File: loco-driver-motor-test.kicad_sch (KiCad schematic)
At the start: 1 part, among them J101 Conn_02x09_Odd_Even

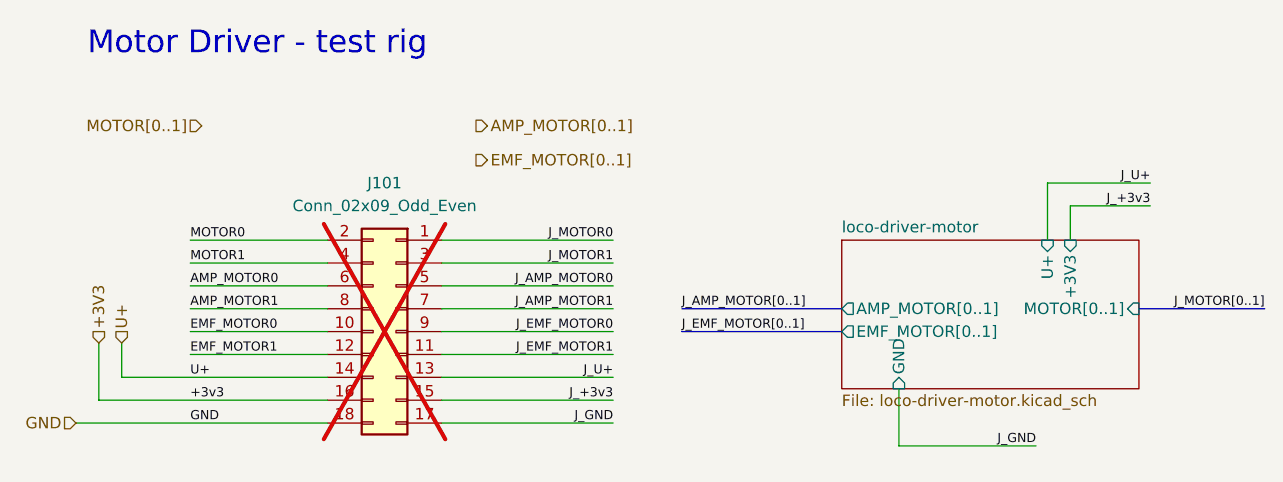
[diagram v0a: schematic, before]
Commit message: Fix - loco-driver-motor-tests pins
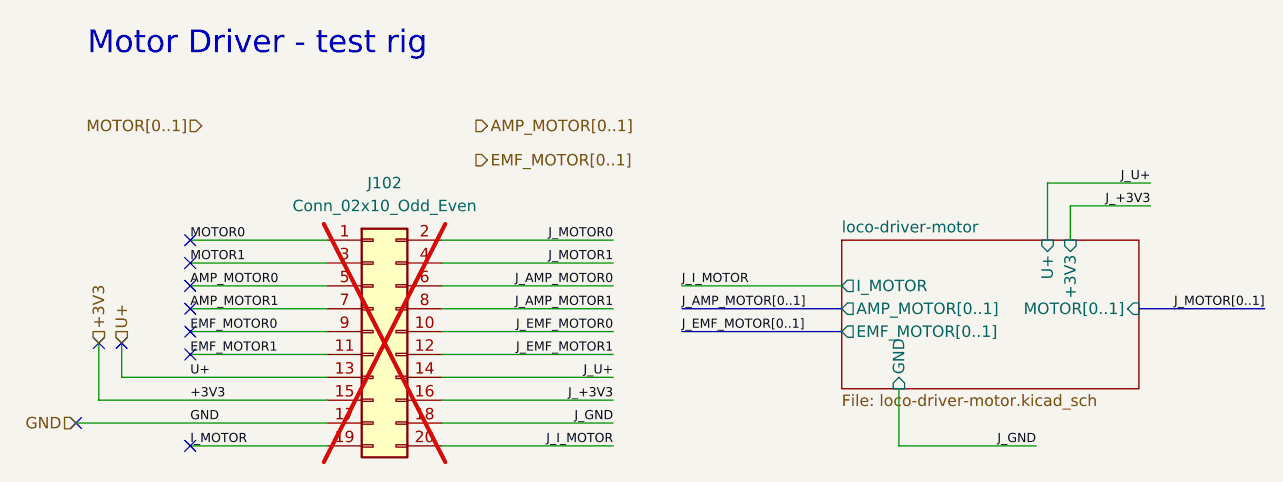
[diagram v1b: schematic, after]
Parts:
- removed J101: Conn_02x09_Odd_Even, Connector_PinSocket_2.54mm:PinSocket_2x09_P2.54mm_Vertical, symbol Connector_Generic:Conn_02x09_Odd_Even
- added J102: Conn_02x10_Odd_Even, Connector_PinSocket_2.54mm:PinSocket_2x10_P2.54mm_Vertical, symbol Connector_Generic:Conn_02x10_Odd_Even
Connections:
- net +3V3: now also J102.15 (Pin_15)
- net AMP_MOTOR0: now also J102.5 (Pin_5)
- net AMP_MOTOR1: now also J102.7 (Pin_7)
- net EMF_MOTOR0: now also J102.9 (Pin_9)
- net EMF_MOTOR1: now also J102.11 (Pin_11)
- net GND: now also J102.17 (Pin_17)
- net J_AMP_MOTOR0: now also J102.6 (Pin_6)
- net J_AMP_MOTOR1: now also J102.8 (Pin_8)
- net J_EMF_MOTOR0: now also J102.10 (Pin_10)
- net J_EMF_MOTOR1: now also J102.12 (Pin_12)
- net J_GND: now also J102.18 (Pin_18)
- net J_MOTOR0: now also J102.2 (Pin_2)
- net J_MOTOR1: now also J102.4 (Pin_4)
- net J_U+: now also J102.14 (Pin_14)
- net MOTOR0: now also J102.1 (Pin_1)
- net MOTOR1: now also J102.3 (Pin_3)
- net U+: now also J102.13 (Pin_13)
- new net I_MOTOR: J102.19 (Pin_19)
- new net J_+3V3: J102.16 (Pin_16)
- new net J_I_MOTOR: J102.20 (Pin_20)
- no-connect marks 0 -> 10
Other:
- sheet loco-driver-motor ports: added I_MOTOR; removed none
